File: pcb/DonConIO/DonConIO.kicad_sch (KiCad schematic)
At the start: 97 parts, among them J1 Ka Left, J2 Don Left, J3 Don Right, J4 Ka Right, J5 Pad, J6 Conn_01x07, J7 Conn_01x07, J8 Conn_02x04_Top_Bottom, J9 Conn_01x03, U1 TL072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

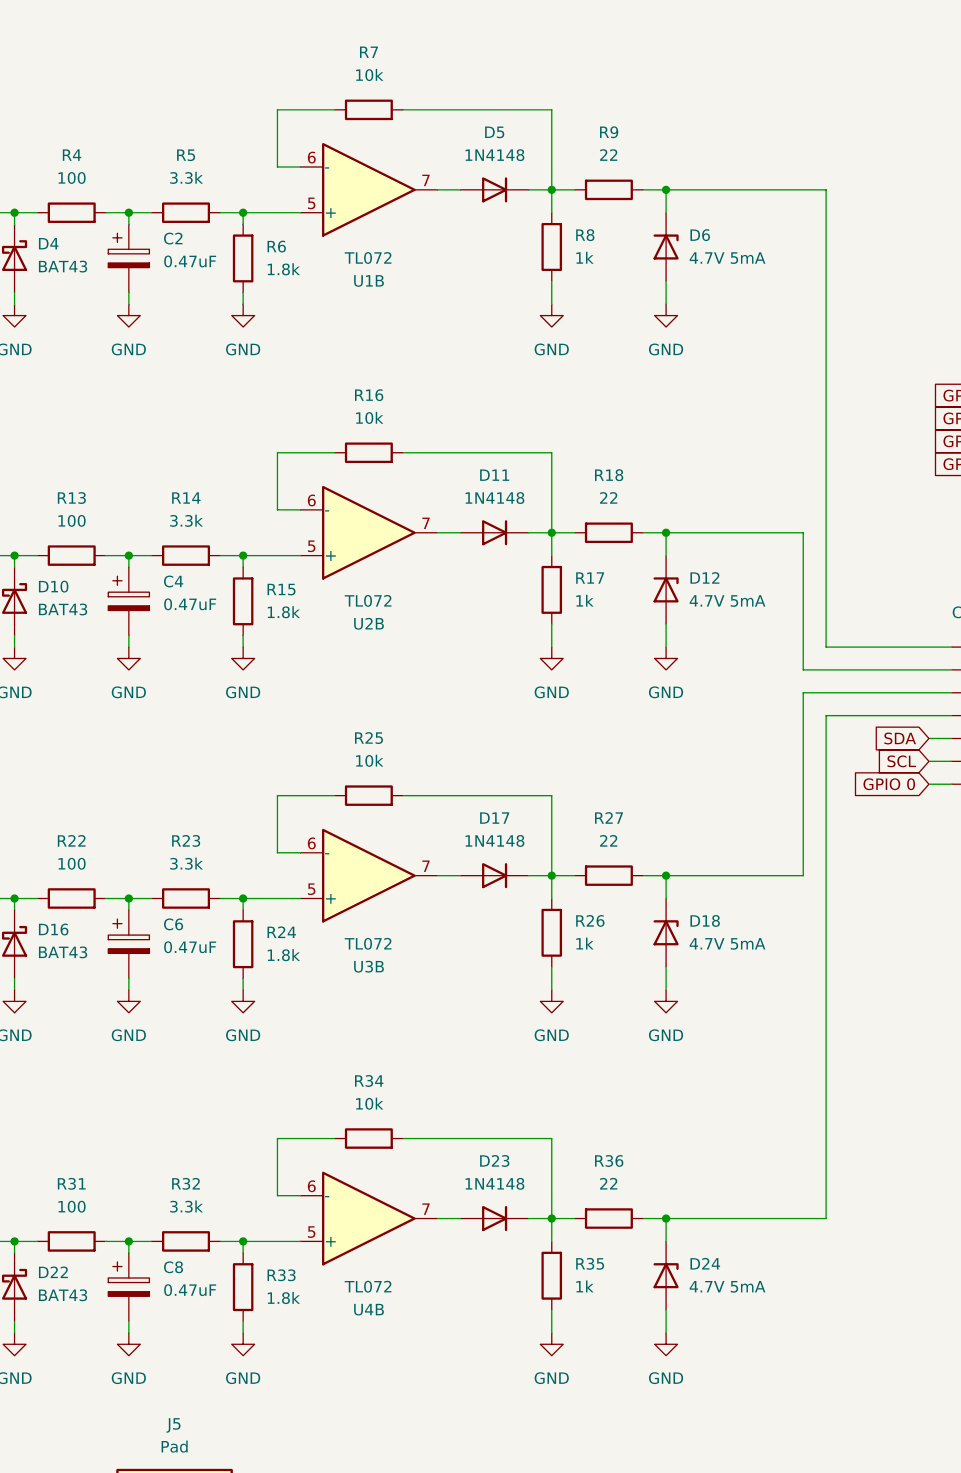
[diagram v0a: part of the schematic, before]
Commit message: Change some resistor values to improve sensitivity
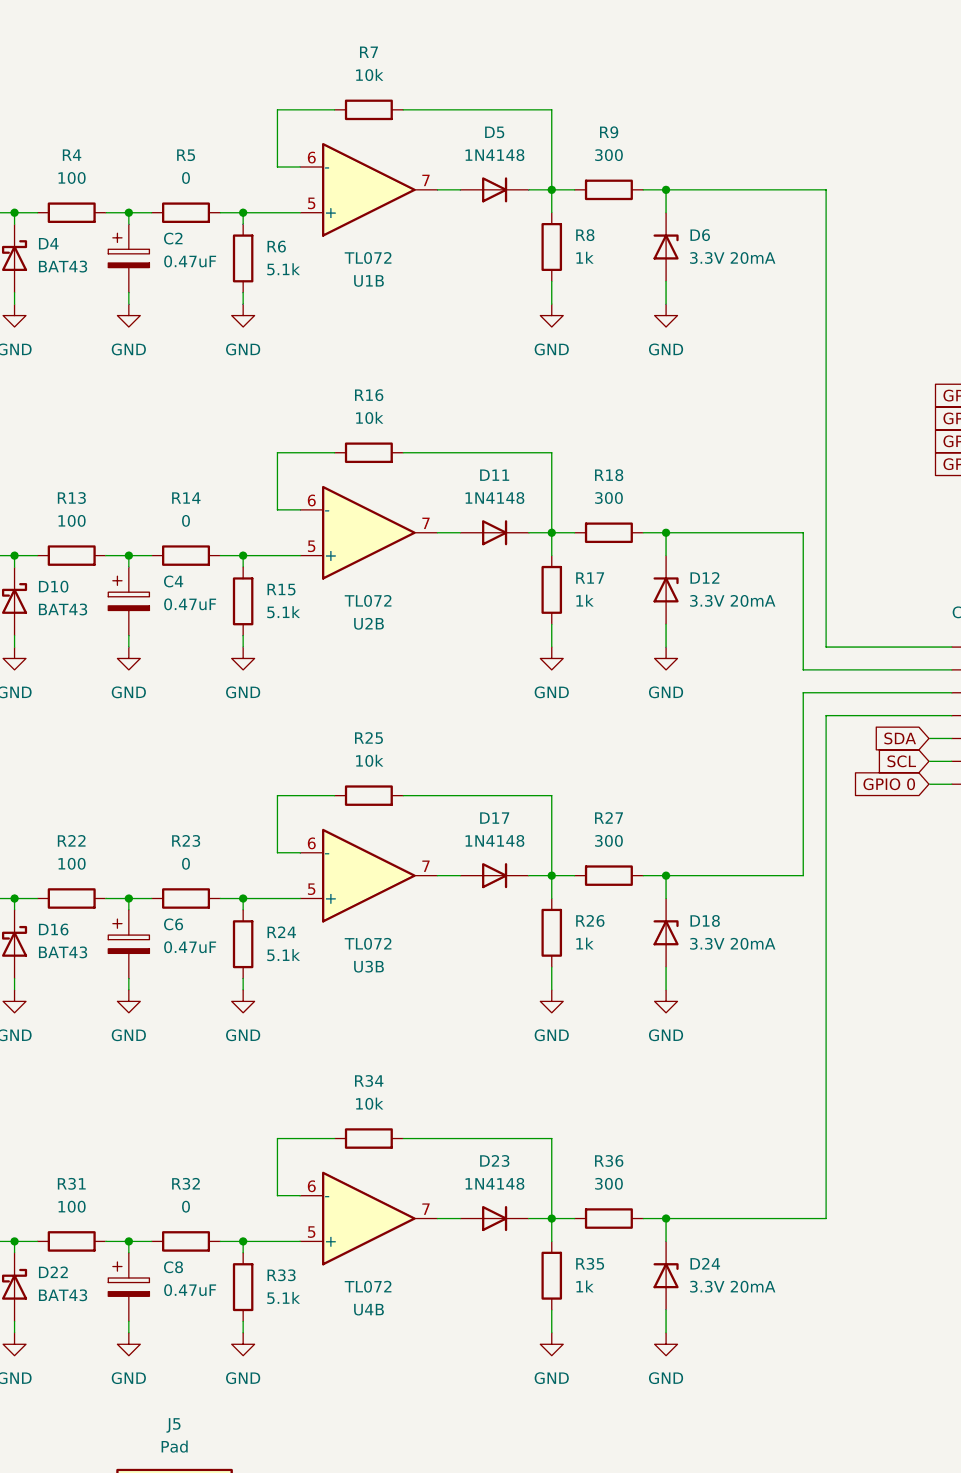
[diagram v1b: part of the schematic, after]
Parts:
- D12, D18, D24, D6: value 4.7V 5mA -> 3.3V 20mA
- R14, R23, R32, R5: value 3.3k -> 0
- R15, R24, R33, R6: value 1.8k -> 5.1k
- R18, R27, R36, R9: value 22 -> 300
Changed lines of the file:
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@@
   (title_block
     (title "DonCon2040")
-    (date "2023-06-19")
-    (rev "2")
+    (date "2023-07-16")
+    (rev "3")
     (company "ravinrabbid")
   )
@@
       (effects (font (size 1.27 1.27)))
     )
-    (property "Value" "22" (at 173.99 105.41 90)
+    (property "Value" "300" (at 173.99 105.41 90)
       (effects (font (size 1.27 1.27)))
     )
@@
       (effects (font (size 1.27 1.27)) (justify right))
     )
-    (property "Value" "1.8k" (at 135.89 41.91 0)
+    (property "Value" "5.1k" (at 135.89 41.91 0)
       (effects (font (size 1.27 1.27)) (justify right))
     )
@@
       (effects (font (size 1.27 1.27)) (justify left))
     )
-    (property "Value" "4.7V 5mA" (at 182.88 116.84 90)
+    (property "Value" "3.3V 20mA" (at 182.88 116.84 90)
       (effects (font (size 1.27 1.27)) (justify left))
     )
@@
       (effects (font (size 1.27 1.27)))
     )
-    (property "Value" "22" (at 173.99 143.51 90)
+    (property "Value" "300" (at 173.99 143.51 90)
       (effects (font (size 1.27 1.27)))
     )
@@
       (effects (font (size 1.27 1.27)))
     )
-    (property "Value" "3.3k" (at 127 31.75 90)
+    (property "Value" "0" (at 127 31.75 90)
       (effects (font (size 1.27 1.27)))
     )
@@
       (effects (font (size 1.27 1.27)) (justify left))
     )
-    (property "Value" "4.7V 5mA" (at 182.88 154.94 90)
+    (property "Value" "3.3V 20mA" (at 182.88 154.94 90)
       (effects (font (size 1.27 1.27)) (justify left))
     )
@@
       (effects (font (size 1.27 1.27)) (justify right))
     )
-    (property "Value" "1.8k" (at 135.89 156.21 0)
+    (property "Value" "5.1k" (at 135.89 156.21 0)
       (effects (font (size 1.27 1.27)) (justify right))
     )
@@
       (effects (font (size 1.27 1.27)) (justify right))
     )
-    (property "Value" "1.8k" (at 135.89 118.11 0)
+    (property "Value" "5.1k" (at 135.89 118.11 0)
       (effects (font (size 1.27 1.27)) (justify right))
     )
@@
       (effects (font (size 1.27 1.27)))
     )
-    (property "Value" "3.3k" (at 127 69.85 90)
+    (property "Value" "0" (at 127 69.85 90)
       (effects (font (size 1.27 1.27)))
     )
@@
       (effects (font (size 1.27 1.27)))
     )
-    (property "Value" "3.3k" (at 127 146.05 90)
+    (property "Value" "0" (at 127 146.05 90)
       (effects (font (size 1.27 1.27)))
     )
@@
       (effects (font (size 1.27 1.27)))
     )
-    (property "Value" "22" (at 173.99 29.21 90)
+    (property "Value" "300" (at 173.99 29.21 90)
       (effects (font (size 1.27 1.27)))
     )
@@
       (effects (font (size 1.27 1.27)))
     )
-    (property "Value" "3.3k" (at 127 107.95 90)
+    (property "Value" "0" (at 127 107.95 90)
       (effects (font (size 1.27 1.27)))
     )
@@
       (effects (font (size 1.27 1.27)))
     )
-    (property "Value" "22" (at 173.99 67.31 90)
+    (property "Value" "300" (at 173.99 67.31 90)
       (effects (font (size 1.27 1.27)))
     )
@@
       (effects (font (size 1.27 1.27)) (justify left))
     )
-    (property "Value" "4.7V 5mA" (at 182.88 40.64 90)
+    (property "Value" "3.3V 20mA" (at 182.88 40.64 90)
       (effects (font (size 1.27 1.27)) (justify left))
     )
@@
       (effects (font (size 1.27 1.27)) (justify right))
     )
-    (property "Value" "1.8k" (at 135.89 80.01 0)
+    (property "Value" "5.1k" (at 135.89 80.01 0)
       (effects (font (size 1.27 1.27)) (justify right))
     )
@@
       (effects (font (size 1.27 1.27)) (justify left))
     )
-    (property "Value" "4.7V 5mA" (at 182.88 78.74 90)
+    (property "Value" "3.3V 20mA" (at 182.88 78.74 90)
       (effects (font (size 1.27 1.27)) (justify left))
     )

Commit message: Add external ADC to DonConIO PCB
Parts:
- removed J8: Conn_02x04_Top_Bottom, Connector_PinHeader_2.54mm:PinHeader_2x04_P2.54mm_Vertical, symbol Connector_Generic:Conn_02x04_Odd_Even
- added C20, C22, C24, C25: 0.1uF, Capacitor_SMD:C_0805_2012Metric_Pad1.18x1.45mm_HandSolder, symbol Device:C_Small
- added C21, C23: 10uF, Capacitor_SMD:C_0805_2012Metric_Pad1.18x1.45mm_HandSolder, symbol Device:C_Small
- added JP1, JP3, JP4: Ka Left, Jumper:SolderJumper-3_P2.0mm_Open_TrianglePad1.0x1.5mm_NumberLabels, symbol Jumper:SolderJumper_3_Open
- added JP2: Don Left, Jumper:SolderJumper-3_P2.0mm_Open_TrianglePad1.0x1.5mm_NumberLabels, symbol Jumper:SolderJumper_3_Open
- added R37: 10k, Resistor_SMD:R_0805_2012Metric_Pad1.20x1.40mm_HandSolder, symbol Device:R_Small
- added U5: MCP3204, Package_SO:SOIC-14_3.9x8.7mm_P1.27mm, symbol Analog_ADC:MCP3204
- added U6: MCP1541-TT, Package_TO_SOT_SMD:SOT-23, symbol Reference_Voltage:MCP1541-TT
- added U7: TXB0104D, Package_SO:SOIC-14_3.9x8.7mm_P1.27mm, symbol Logic_LevelTranslator:TXB0104D
- D12, D18, D24: value 3.3V 20mA -> 4.3V
- D6: value 3.3V 20mA -> 4.1V
- J6: value Conn_01x07 -> MCU1
- J7: value Conn_01x07 -> MCU2
- J9: value Conn_01x03 -> Power 12V
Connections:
- net +3V3: now also C24.1, U7.1 (VCCA)
- net +5V: now also C20.2, C22.2, C23.2, C25.2, U5.14 (Vdd), U6.1 (Vin), U7.14 (VCCB)
- net GND: now also C20.1, C21.1, C22.1, C23.1, C24.2, C25.1, R37.2, U5.12 (AGND), U5.7 (DGND), U6.3 (Vss), U7.7 (GND)
- net at D18.1 (K), R27.1: now also JP3.2 (C); no longer J6.3 (Pin_3)
- net at D6.1 (K), R9.1: now also JP1.2 (C); no longer J6.1 (Pin_1)
- net at D12.1 (K), R18.1: now also JP2.2 (C); no longer J6.2 (Pin_2)
- net at D24.1 (K), R36.1: now also JP4.2 (C); no longer J6.4 (Pin_4)
- net Don_Left renamed Don_Left_IN
- net Don_Right renamed Don_Right_IN
- net GPIO 0 renamed SPI OE
- net SPI OE: now also R37.1, U7.8 (OE)
- net GPIO 1 renamed SPI nCS
- net SPI nCS: now also U7.2 (A1)
- net GPIO 2 renamed SPI SCLK
- net SPI SCLK: now also U7.3 (A2)
- net GPIO 3 renamed SPI MOSI
- net SPI MOSI: now also U7.5 (A4)
- net GPIO 4 renamed SPI MISO
- net SPI MISO: now also U7.4 (A3)
- net Ka_Left renamed Ka_Left_IN
- net Ka_Right renamed Ka_Right_IN
- new net: U5.9 (Din), U7.10 (B4)
- new net: U5.10 (Dout), U7.11 (B3)
- new net: U5.11 (CLK), U7.12 (B2)
- new net: U5.8 (~{CS}/SHDN), U7.13 (B1)
- new net: C21.2, U5.13 (Vref), U6.2 (Vout)
- new net Don_Left_ADC: JP2.3 (B), U5.2 (CH1)
- new net Don_Left_DIRECT: J6.2 (Pin_2), JP2.1 (A)
- new net Don_Right_ADC: JP3.3 (B), U5.3 (CH2)
- new net Don_Right_DIRECT: J6.3 (Pin_3), JP3.1 (A)
- new net Ka_Left_ADC: JP1.3 (B), U5.1 (CH0)
- new net Ka_Left_DIRECT: J6.1 (Pin_1), JP1.1 (A)
- new net Ka_Right_ADC: JP4.3 (B), U5.4 (CH3)
- new net Ka_Right_DIRECT: J6.4 (Pin_4), JP4.1 (A)
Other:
- moved on the sheet: C17, C18, C19, H1, H2, H3, H4, J1, J2, J3, J4, J5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

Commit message: Add missing level shifter to IO board
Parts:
- removed J9: Power 12V, Connector_PinHeader_2.54mm:PinHeader_1x03_P2.54mm_Vertical, symbol Connector_Generic:Conn_01x03
- removed JP1, JP3, JP4: Ka Left, Jumper:SolderJumper-3_P2.0mm_Open_TrianglePad1.0x1.5mm_NumberLabels, symbol Jumper:SolderJumper_3_Open
- removed JP2: Don Left, Jumper:SolderJumper-3_P2.0mm_Open_TrianglePad1.0x1.5mm_NumberLabels, symbol Jumper:SolderJumper_3_Open
- removed R14, R23, R32, R5: 0, Resistor_THT:R_Axial_DIN0207_L6.3mm_D2.5mm_P7.62mm_Horizontal, symbol Device:R
- added C26: 10uF, Capacitor_SMD:C_0805_2012Metric_Pad1.18x1.45mm_HandSolder, symbol Device:C_Small
- added J8: GPIO/ADC, Connector_PinHeader_2.54mm:PinHeader_2x04_P2.54mm_Vertical, symbol Connector_Generic:Conn_02x04_Odd_Even
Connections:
- net +3V3: now also C26.2
- net Don_Left_ADC: now also D12.1 (K), R18.1
- net Don_Right_ADC: now also D18.1 (K), R27.1
- net GND: now also C26.1, J8.1 (Pin_1), J8.3 (Pin_3), J8.5 (Pin_5), J8.7 (Pin_7)
- net Ka_Left_ADC: now also D6.1 (K), R9.1
- net Ka_Right_ADC: now also D24.1 (K), R36.1
- net SPI MOSI: now also U7.3 (A2); no longer U7.5 (A4)
- net SPI SCLK: now also U7.5 (A4); no longer U7.3 (A2)
- net at R24.2, U3.5 (+): now also C6.1, R22.2
- net at R15.2, U2.5 (+): now also C4.1, R13.2
- net at R6.2, U1.5 (+): now also C2.1, R4.2
- net at R33.2, U4.5 (+): now also C8.1, R31.2
- net at U7.10 (B4): now also U5.11 (CLK); no longer U5.9 (Din)
- net at U7.12 (B2): now also U5.9 (Din); no longer U5.11 (CLK)
- net Don_Left_DIRECT: no longer names the net of J6.2 (Pin_2)
- net Don_Left_DIRECT: now also J8.4 (Pin_4)
- net Don_Right_DIRECT: no longer names the net of J6.3 (Pin_3)
- net Don_Right_DIRECT: now also J8.6 (Pin_6)
- net Ka_Left_DIRECT: no longer names the net of J6.1 (Pin_1)
- net Ka_Left_DIRECT: now also J8.2 (Pin_2)
- net Ka_Right_DIRECT: no longer names the net of J6.4 (Pin_4)
- net Ka_Right_DIRECT: now also J8.8 (Pin_8)
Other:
- moved on the sheet: C23, J6, J7

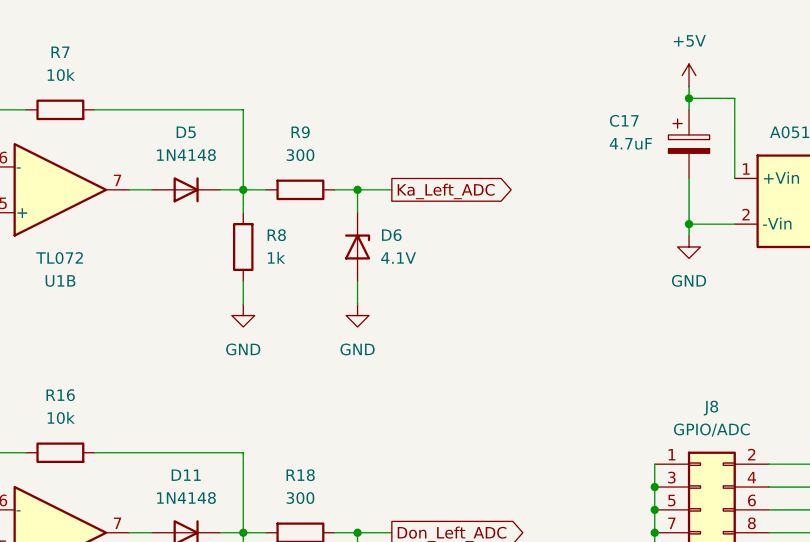
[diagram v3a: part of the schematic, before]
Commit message: Export IO board schematic pdf
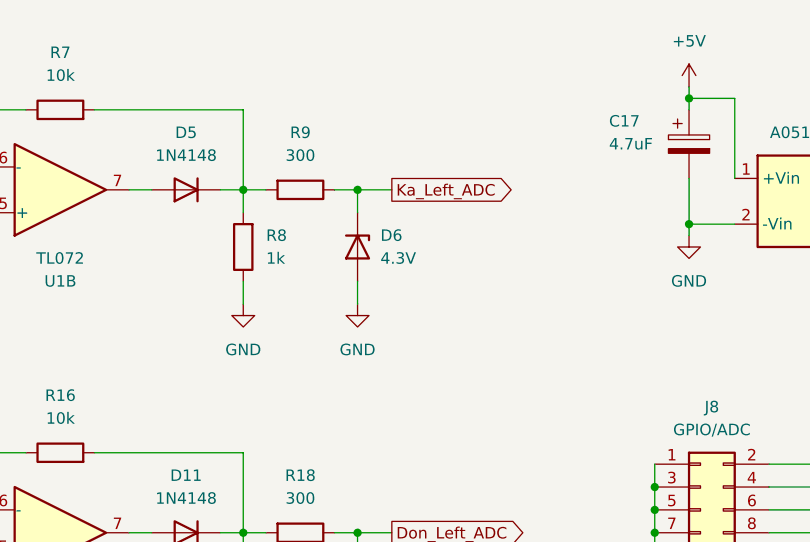
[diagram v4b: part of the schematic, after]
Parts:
- D6: value 4.1V -> 4.3V
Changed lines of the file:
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@@
       (effects (font (size 1.27 1.27)) (justify left))
     )
-    (property "Value" "4.1V" (at 182.88 40.64 90)
+    (property "Value" "4.3V" (at 182.88 40.64 90)
       (effects (font (size 1.27 1.27)) (justify left))
     )
